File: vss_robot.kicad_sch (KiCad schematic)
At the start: 14 parts, among them J2 Conn_01x04_Socket, J3 Conn_01x02_Socket, J4 Conn_01x02_Socket, J5 Conn_01x06_Socket, SW1 SW_Push, U1 LM1117DT-3.3, U2 NRF24L01_Breakout, U4 ESP32-DEVKIT-V1

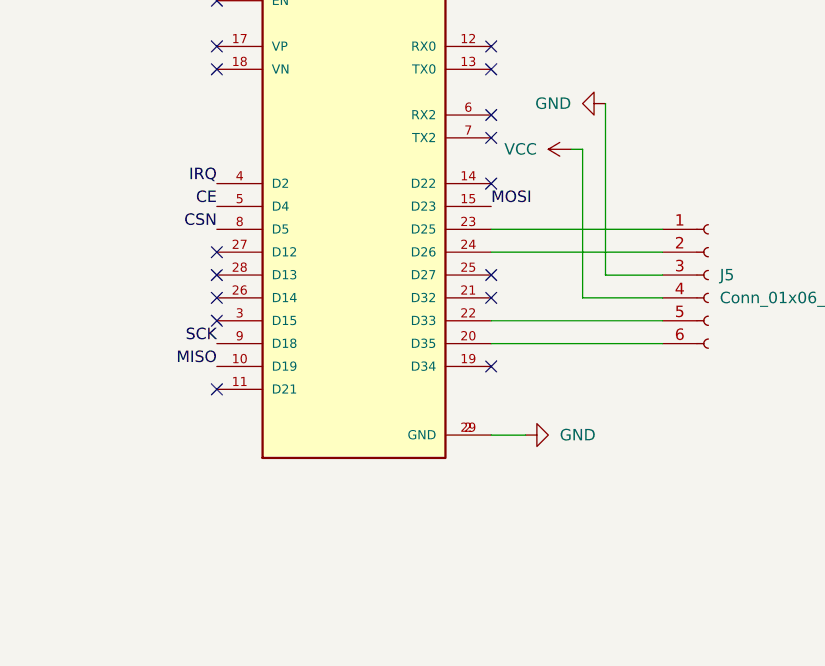
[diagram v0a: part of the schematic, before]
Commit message: grossura da trilha, layer e posicionamento
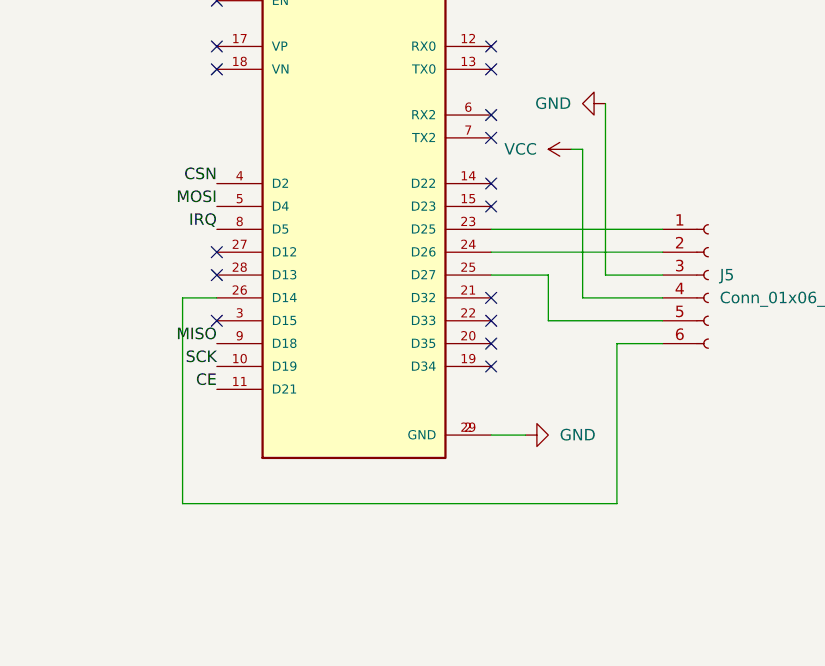
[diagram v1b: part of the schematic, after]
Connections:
- net CE: now also U4.11 (D21); no longer U4.5 (D4)
- net CSN: now also U4.4 (D2); no longer U4.8 (D5)
- net IRQ: now also U4.8 (D5); no longer U4.4 (D2)
- net MISO: now also U4.9 (D18); no longer U4.10 (D19)
- net MOSI: now also U4.5 (D4); no longer U4.15 (D23)
- net SCK: now also U4.10 (D19); no longer U4.9 (D18)
- net at J5.5 (Pin_5): now also U4.25 (D27); no longer U4.22 (D33)
- net at J5.6 (Pin_6): now also U4.26 (D14); no longer U4.20 (D35)
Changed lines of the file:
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@@
-	)
-	(no_connect
-		(at 152.4 114.3)
 	)
 	(no_connect
@@
 	)
 	(no_connect
+		(at 121.92 119.38)
+	)
+	(no_connect
 		(at 152.4 104.14)
 	)
 	(no_connect
+		(at 152.4 81.28)
+	)
+	(no_connect
 		(at 121.92 114.3)
 	)
 	(no_connect
-		(at 152.4 81.28)
+		(at 152.4 106.68)
 	)
 	(no_connect
@@
 	)
 	(no_connect
+		(at 152.4 121.92)
+	)
+	(no_connect
 		(at 152.4 124.46)
 	)
 	(no_connect
+		(at 121.92 111.76)
+	)
+	(no_connect
 		(at 152.4 88.9)
 	)
 	(no_connect
+		(at 121.92 88.9)
+	)
+	(no_connect
 		(at 152.4 116.84)
 	)
 	(no_connect
-		(at 121.92 119.38)
-	)
-	(no_connect
-		(at 121.92 127)
-	)
-	(no_connect
-		(at 121.92 116.84)
-	)
-	(no_connect
-		(at 121.92 88.9)
-	)
-	(no_connect
-		(at 121.92 111.76)
-	)
-	(no_connect
 		(at 152.4 96.52)
 	)
+	(no_connect
+		(at 152.4 119.38)
+	)
+	(wire
+		(pts
+			(xy 158.75 114.3) (xy 152.4 114.3)
+		)
+		(stroke
+			(width 0)
+			(type default)
+		)
+	)
 	(wire
 		(pts
@@
 	(wire
 		(pts
-			(xy 152.4 121.92) (xy 171.45 121.92)
-		)
-		(stroke
-			(width 0)
-			(type default)
-		)
-	)
-	(wire
-		(pts
 			(xy 116.84 21.59) (xy 133.35 21.59)
 		)
@@
 	(wire
 		(pts
+			(xy 118.11 116.84) (xy 121.92 116.84)
+		)
+		(stroke
+			(width 0)
+			(type default)
+		)
+	)
+	(wire
+		(pts
 			(xy 208.28 119.38) (xy 228.6 119.38)
 		)
@@
 	(wire
 		(pts
+			(xy 166.37 139.7) (xy 118.11 139.7)
+		)
+		(stroke
+			(width 0)
+			(type default)
+		)
+	)
+	(wire
+		(pts
 			(xy 80.01 25.4) (xy 80.01 31.75)
 		)
@@
 	(wire
 		(pts
+			(xy 158.75 119.38) (xy 171.45 119.38)
+		)
+		(stroke
+			(width 0)
+			(type default)
+		)
+	)
+	(wire
+		(pts
 			(xy 165.1 114.3) (xy 165.1 95.25)
 		)
@@
 	(wire
 		(pts
+			(xy 171.45 121.92) (xy 166.37 121.92)
+		)
+		(stroke
+			(width 0)
+			(type default)
+		)
+	)
+	(wire
+		(pts
 			(xy 24.13 62.23) (xy 24.13 68.58)
 		)
@@
 	(wire
 		(pts
+			(xy 166.37 121.92) (xy 166.37 139.7)
+		)
+		(stroke
+			(width 0)
+			(type default)
+		)
+	)
+	(wire
+		(pts
 			(xy 80.01 25.4) (xy 95.25 25.4)
 		)
@@
 	(wire
 		(pts
-			(xy 152.4 119.38) (xy 171.45 119.38)
-		)
-		(stroke
-			(width 0)
-			(type default)
-		)
-	)
-	(wire
-		(pts
 			(xy 83.82 83.82) (xy 83.82 90.17)
 		)
@@
 	(wire
 		(pts
+			(xy 118.11 139.7) (xy 118.11 116.84)
+		)
+		(stroke
+			(width 0)
+			(type default)
+		)
+	)
+	(wire
+		(pts
 			(xy 71.12 83.82) (xy 71.12 87.63)
+		)
+		(stroke
+			(width 0)
+			(type default)
+		)
+	)
+	(wire
+		(pts
+			(xy 158.75 114.3) (xy 158.75 119.38)
 		)
 		(stroke
@@
 		)
 	)
+	(label "MISO"
+		(at 121.92 121.92 180)
+		(fields_autoplaced yes)
+		(effects
+			(font
+				(size 1.27 1.27)
+			)
+			(justify right bottom)
+		)
+	)
 	(label "CE"
 		(at 223.52 55.88 180)
@@
 		)
 	)
-	(label "IRQ"
-		(at 121.92 104.14 180)
+	(label "MOSI"
+		(at 121.92 106.68 180)
+		(fields_autoplaced yes)
+		(effects
+			(font
+				(size 1.27 1.27)
+			)
+			(justify right bottom)
+		)
+	)
+	(label "SCK"
+		(at 121.92 124.46 180)
 		(fields_autoplaced yes)
 		(effects
@@
 		)
 	)
-	(label "CE"
-		(at 121.92 106.68 180)
-		(fields_autoplaced yes)
-		(effects
-			(font
-				(size 1.27 1.27)
-			)
-			(justify right bottom)
-		)
-	)
 	(label "MOSI"
 		(at 223.52 43.18 180)
@@
 	)
 	(label "CSN"
+		(at 121.92 104.14 180)
+		(fields_autoplaced yes)
+		(effects
+			(font
+				(size 1.27 1.27)
+			)
+			(justify right bottom)
+		)
+	)
+	(label "IRQ"
 		(at 121.92 109.22 180)
 		(fields_autoplaced yes)
@@
 		)
 	)
-	(label "MISO"
-		(at 121.92 124.46 180)
-		(fields_autoplaced yes)
-		(effects
-			(font
-				(size 1.27 1.27)
-			)
-			(justify right bottom)
-		)
-	)
-	(label "MOSI"
-		(at 152.4 106.68 0)
-		(fields_autoplaced yes)
-		(effects
-			(font
-				(size 1.27 1.27)
-			)
-			(justify left bottom)
-		)
-	)
-	(label "SCK"
-		(at 121.92 121.92 180)
-		(fields_autoplaced yes)
-		(effects
+	(label "CE"
+		(at 121.92 127 180)
+		(fields_autoplaced yes)
+		(effects
